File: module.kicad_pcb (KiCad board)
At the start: 2 copper layers, 99 x 84.2 mm, 14 parts, among them J10 Screw_Terminal_01x05, J11 Screw_Terminal_01x05, J7 Screw_Terminal_01x02, J8 Screw_Terminal_01x02, J9 Screw_Terminal_01x02, U1 L7812

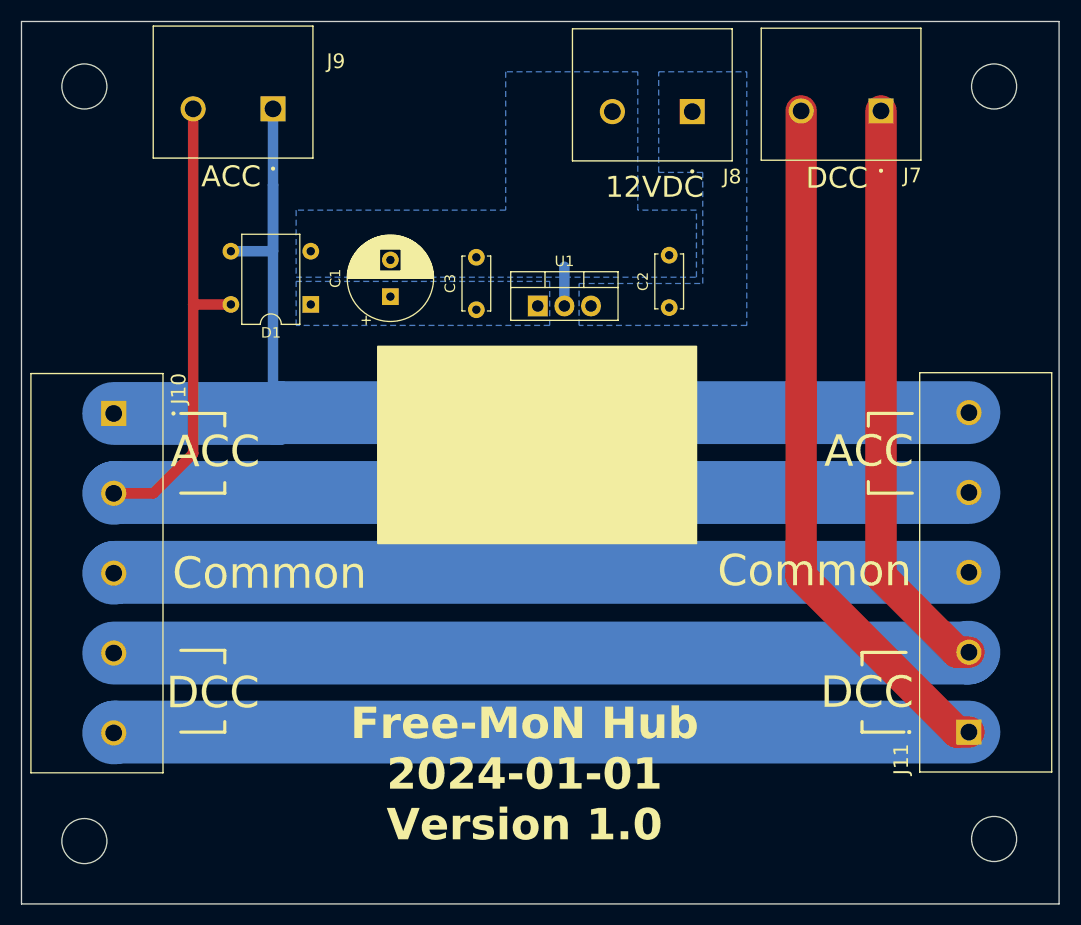
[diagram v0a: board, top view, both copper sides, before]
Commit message: Added the +/- and N/S indications to the silk layer
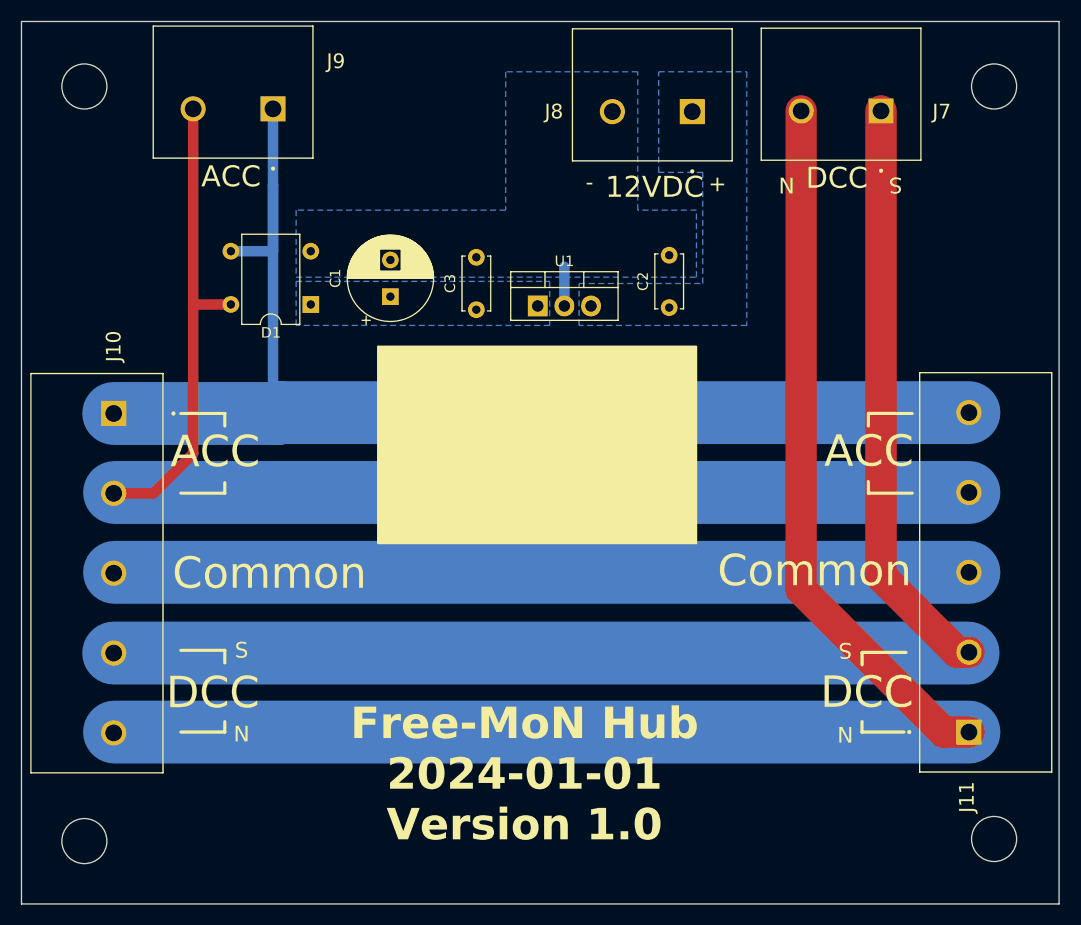
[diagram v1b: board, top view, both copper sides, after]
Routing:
- net Net-(J10-Pin_5): track 148.2 -> 148.8 mm
- net Net-(J10-Pin_1): track 121.2 -> 120.6 mm
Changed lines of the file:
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@@
     (property "ki_keywords" "screw terminal")
     (attr through_hole)
-    (fp_text reference "J8" (at -3.8 -6.2) (layer "F.SilkS")
+    (fp_text reference "J8" (at 13.2 0) (layer "F.SilkS")
         (effects (font (size 1.4 1.4) (thickness 0.15)))
     )
@@
     (fp_text user "${Label}" (at 3.6 -7.2) (layer "F.SilkS")
         (effects (font (size 2 2) (thickness 0.3)))
+    )
+    (fp_text user "+" (at -2.4 -7 180 unlocked) (layer "F.SilkS")
+        (effects (font (size 1.5 1.5) (thickness 0.2)))
+    )
+    (fp_text user "-" (at 9.8 -7 180 unlocked) (layer "F.SilkS")
+        (effects (font (size 1.5 1.5) (thickness 0.2)))
     )
     (fp_line (start -3.81 -4.7) (end 11.43 -4.7)
@@
     (property "ki_keywords" "screw terminal")
     (attr through_hole)
-    (fp_text reference "J11" (at -2.6 -6.4625 90) (layer "F.SilkS")
+    (fp_text reference "J11" (at -6.2 -0.2 90) (layer "F.SilkS")
         (effects (font (size 1.4 1.4) (thickness 0.15)))
     )
@@
         (effects (font (size 1.4 1.4) (thickness 0.15)))
     )
+    (fp_text user "S" (at 7.8 -11.8 180 unlocked) (layer "F.SilkS")
+        (effects (font (size 1.5 1.5) (thickness 0.2)))
+    )
     (fp_text user "ACC" (at 26.8 -5.2625 unlocked) (layer "F.SilkS")
         (effects (font (size 3 3) (thickness 0.5)) (justify right))
+    )
+    (fp_text user "N" (at -0.2 -11.8 180 unlocked) (layer "F.SilkS")
+        (effects (font (size 1.5 1.5) (thickness 0.2)))
     )
     (fp_text user "DCC" (at 3.8 -5.2625 unlocked) (layer "F.SilkS")
@@
     (property "ki_keywords" "screw terminal")
     (attr through_hole)
-    (fp_text reference "J10" (at -2.36 -6.2 90) (layer "F.SilkS")
+    (fp_text reference "J10" (at -6.4 0 90) (layer "F.SilkS")
         (effects (font (size 1.4 1.4) (thickness 0.15)))
     )
     (fp_text value "Screw_Terminal_01x05" (at 11.192 9.261 90) (layer "F.Fab")
         (effects (font (size 1.4 1.4) (thickness 0.15)))
+    )
+    (fp_text user "S" (at 22.6 -12.2 unlocked) (layer "F.SilkS")
+        (effects (font (size 1.5 1.5) (thickness 0.2)))
+    )
+    (fp_text user "N" (at 30.6 -12.2 unlocked) (layer "F.SilkS")
+        (effects (font (size 1.5 1.5) (thickness 0.2)))
     )
     (fp_text user "Common" (at 15.24 -5.6 unlocked) (layer "F.SilkS")
@@
     (property "ki_keywords" "screw terminal")
     (attr through_hole)
-    (fp_text reference "J7" (at -2.99 -6.16) (layer "F.SilkS")
+    (fp_text reference "J7" (at -5.79 -0.0625) (layer "F.SilkS")
         (effects (font (size 1.4 1.4) (thickness 0.15)))
     )
@@
     (fp_text user "${Label}" (at 4.21 -6.4) (layer "F.SilkS")
         (effects (font (size 2 2) (thickness 0.3)))
+    )
+    (fp_text user "S" (at -1.39 -7.0625 180 unlocked) (layer "F.SilkS")
+        (effects (font (size 1.5 1.5) (thickness 0.2)))
+    )
+    (fp_text user "N" (at 9.01 -7.0625 180 unlocked) (layer "F.SilkS")
+        (effects (font (size 1.5 1.5) (thickness 0.2)))
     )
     (fp_line (start -3.81 -4.7) (end 11.43 -4.7)
@@
   (segment (start 190.4 109.98) (end 189.2625 109.98) (width 3) (layer "F.Cu") (net 3))
   (segment (start 108.8 110.06) (end 190.32 110.06) (width 6) (layer "B.Cu") (net 3))
-  (segment (start 190.32 110.06) (end 190.4 109.98) (width 6) (layer "B.Cu") (net 3))
-  (segment (start 189.2625 117.6) (end 174.39 102.7275) (width 3) (layer "F.Cu") (net 4))
-  (segment (start 174.39 102.7275) (end 174.39 58.3375) (width 3) (layer "F.Cu") (net 4))
-  (segment (start 190.4 117.6) (end 189.2625 117.6) (width 3) (layer "F.Cu") (net 4))
-  (segment (start 108.88 117.6) (end 108.8 117.68) (width 6) (layer "B.Cu") (net 4))
+  (segment (start 188 117.6) (end 174.39 103.99) (width 3) (layer "F.Cu") (net 4))
+  (segment (start 174.39 103.99) (end 174.39 58.3375) (width 3) (layer "F.Cu") (net 4))
+  (segment (start 190.4 117.6) (end 188 117.6) (width 3) (layer "F.Cu") (net 4))
   (segment (start 190.4 117.6) (end 108.88 117.6) (width 6) (layer "B.Cu") (net 4))
   (segment (start 124.44 87.2) (end 108.8 87.2) (width 6) (layer "B.Cu") (net 5))
   (segment (start 119.98 71.72) (end 124 71.72) (width 1) (layer "B.Cu") (net 5))
+  (segment (start 124.52 87.12) (end 190.4 87.12) (width 6) (layer "B.Cu") (net 5))
   (segment (start 124 86.76) (end 124 65.4) (width 1) (layer "B.Cu") (net 5))
+  (segment (start 124.44 87.2) (end 124.52 87.12) (width 6) (layer "B.Cu") (net 5))
   (segment (start 124 71.72) (end 124 65.4) (width 1) (layer "B.Cu") (net 5))
-  (segment (start 124.44 87.2) (end 124 86.76) (width 1) (layer "B.Cu") (net 5))
-  (segment (start 124.44 87.2) (end 124.52 87.12) (width 6) (layer "B.Cu") (net 5))
-  (segment (start 124.52 87.12) (end 190.4 87.12) (width 6) (layer "B.Cu") (net 5))
   (segment (start 124 58.1375) (end 124 65.4) (width 1) (layer "B.Cu") (net 5))
   (segment (start 116.4 76.8) (end 116.38 76.78) (width 1) (layer "F.Cu") (net 6))
@@
   (segment (start 112.58 94.82) (end 116.38 91.02) (width 1) (layer "F.Cu") (net 6))
   (segment (start 190.4 94.74) (end 108.88 94.74) (width 6) (layer "B.Cu") (net 6))
-  (segment (start 108.88 94.74) (end 108.8 94.82) (width 6) (layer "B.Cu") (net 6))
   (segment (start 190.4 102.36) (end 108.88 102.36) (width 6) (layer "B.Cu") (net 7))
-  (segment (start 108.88 102.36) (end 108.8 102.44) (width 6) (layer "B.Cu") (net 7))
   (zone (net 1) (net_name "Net-(D1--)") (layer "B.Cu") (hatch edge 0.5)
     (connect_pads (clearance 0.5))

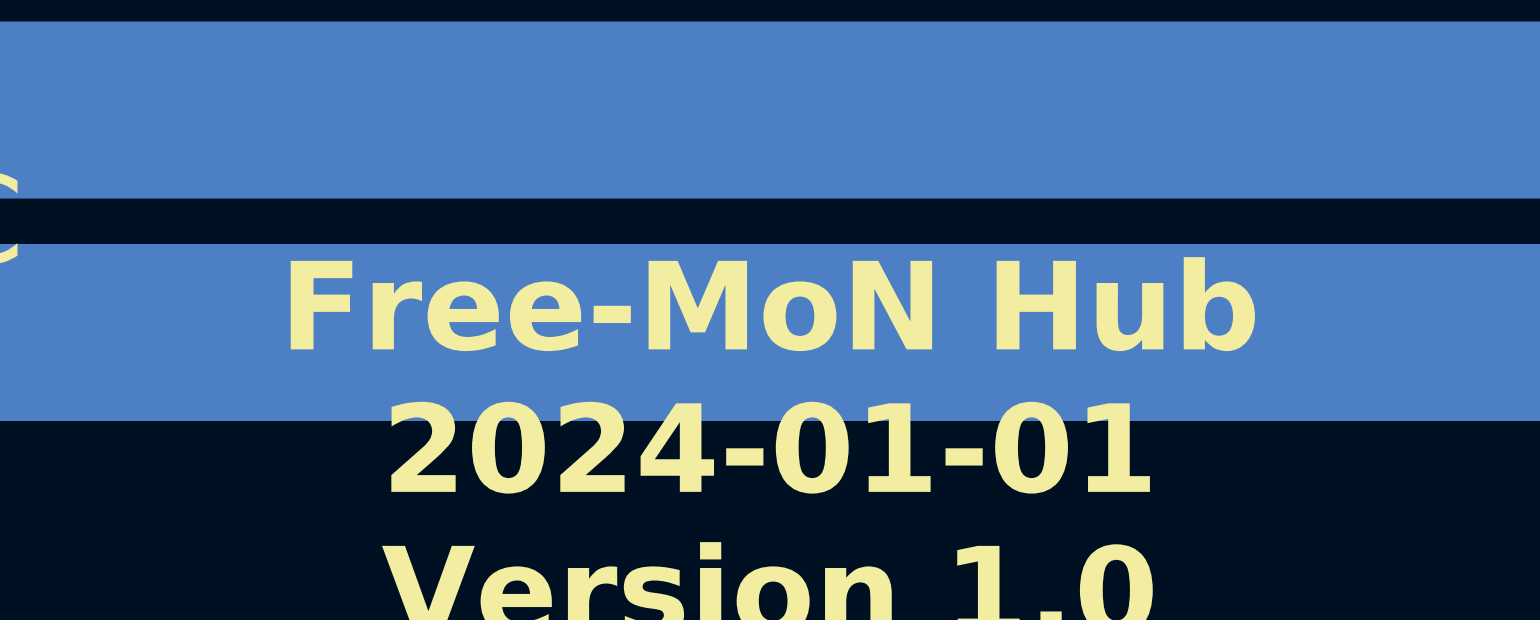
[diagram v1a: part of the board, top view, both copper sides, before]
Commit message: Corrected spelling of Free-moN
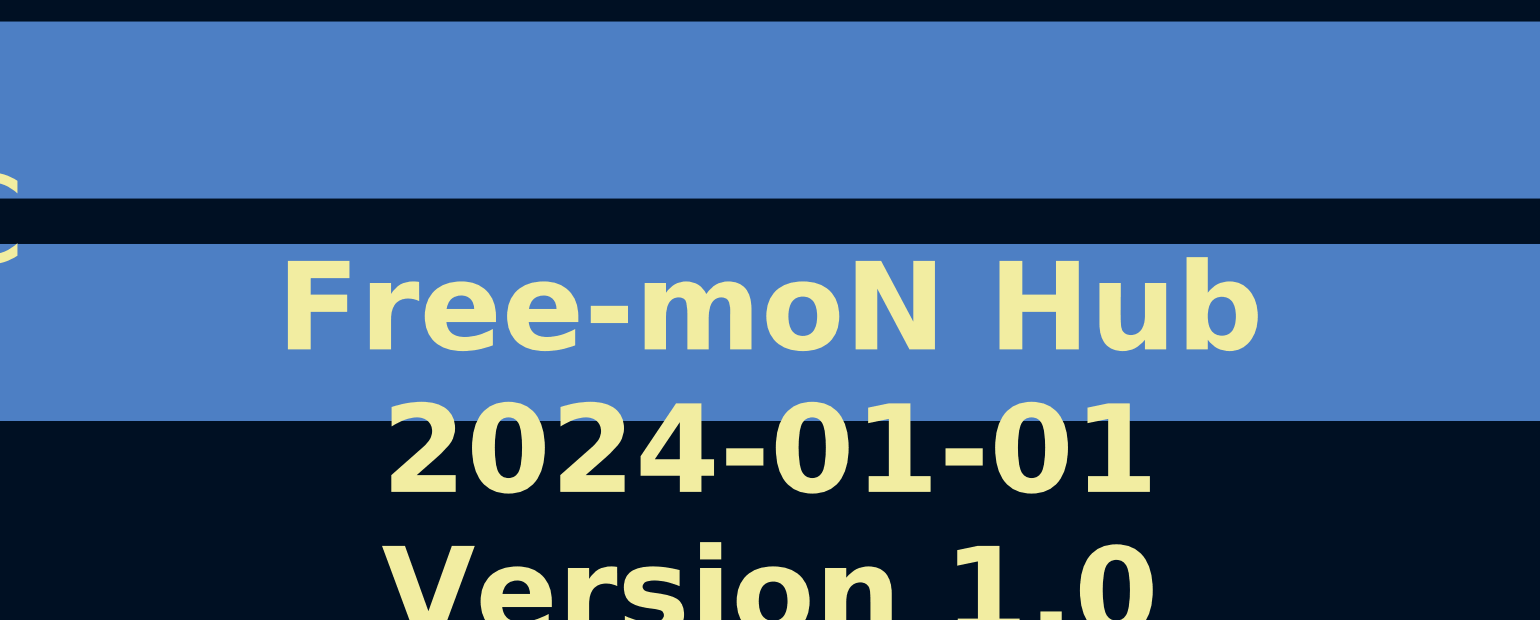
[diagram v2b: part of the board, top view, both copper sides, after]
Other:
- board text added: "Free-moN Hub ${ISSUE_DATE} Version ${REVISION}"
- board text removed: "Free-MoN Hub ${ISSUE_DATE} Version ${REVISION}"
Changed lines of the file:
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@@
   (gr_rect (start 100 49.8) (end 199 134)
     (stroke (width 0.1) (type default)) (fill none) (layer "Edge.Cuts"))
-  (gr_text "Free-MoN Hub\n${ISSUE_DATE}\nVersion ${REVISION}" (at 148 128.2) (layer "F.SilkS")
+  (gr_text "Free-moN Hub\n${ISSUE_DATE}\nVersion ${REVISION}" (at 148 128.2) (layer "F.SilkS")
     (effects (font (size 3 3) (thickness 0.7) bold) (justify bottom))
   )
